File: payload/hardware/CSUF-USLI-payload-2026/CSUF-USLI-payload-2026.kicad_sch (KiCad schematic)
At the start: 1 part, among them U1 DEV-16771

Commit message: made some changes
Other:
- note added: "Leg Subsystem"
- note added: "Power Subsystem"
- note added: "Rover Subsystem"
- note added: "Sensor Subsystem"
- note added: "UTG Payload"
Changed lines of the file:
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@@
+		)
+	)
+	(polyline
+		(pts
+			(xy 284.48 59.69) (xy 284.48 59.69)
+		)
+		(stroke
+			(width 0.5)
+			(type default)
 		)
 	)
@@
 	(polyline
 		(pts
+			(xy 11.43 101.6) (xy 123.19 101.6)
+		)
+		(stroke
+			(width 0.5)
+			(type default)
+		)
+	)
+	(polyline
+		(pts
+			(xy 196.85 59.69) (xy 284.48 59.69)
+		)
+		(stroke
+			(width 0.5)
+			(type default)
+		)
+	)
+	(polyline
+		(pts
+			(xy 196.85 59.69) (xy 201.93 59.69)
+		)
+		(stroke
+			(width 0.5)
+			(type default)
+		)
+	)
+	(polyline
+		(pts
 			(xy 123.19 12.7) (xy 123.19 127)
 		)
@@
 		(effects
 			(font
+				(size 1.27 1.27)
+			)
+		)
+	)
+	(text "Rover Subsystem"
+		(exclude_from_sim no)
+		(at 37.084 177.292 0)
+		(effects
+			(font
+				(size 1.27 1.27)
+			)
+		)
+	)
+	(text "Power Subsystem"
+		(exclude_from_sim no)
+		(at 241.3 57.658 0)
+		(effects
+			(font
+				(size 1.27 1.27)
+			)
+		)
+	)
+	(text "Sensor Subsystem"
+		(exclude_from_sim no)
+		(at 69.85 97.79 0)
+		(effects
+			(font
+				(size 1.27 1.27)
+			)
+		)
+	)
+	(text "Leg Subsystem\n"
+		(exclude_from_sim no)
+		(at 37.338 182.372 0)
+		(effects
+			(font
+				(size 1.27 1.27)
+			)
+		)
+	)
+	(text "UTG Payload\n"
+		(exclude_from_sim no)
+		(at 193.548 189.992 0)
+		(effects
+			(font

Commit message: asdAdded changes n stuff
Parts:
- added BZ1: Buzzer, symbol Device:Buzzer
- added U2: GPS6MV2, symbol GPS6MV2:GPS6MV2
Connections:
- net +3V3: now also U2.1 (Vin)
- net GND: now also BZ1.2 (-), U2.4 (GND)
- net NEO6M_RX: now also U2.2 (RX)
- net NEO6M_TX: now also U2.3 (TX)
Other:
- note added: "I/O Subsystem"
- note removed: "Sensor Subsystem"

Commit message: Motor Diagram Concept
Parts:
- added D1: 12V Drill, symbol L298N Concept:12V_Drill
- added L1: L298N DualDC Motor Driver, symbol L298N Concept:L298N
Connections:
- net GND: now also L1. (Input1)
- new net: D1. (M2), L1. (Input1) (x2)
- new net 12V: L1. (Input1)
- new net Input1: L1. (Input1)
- new net Input2: L1. (Input1)
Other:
- note added: "Drill Controller Subsystem"

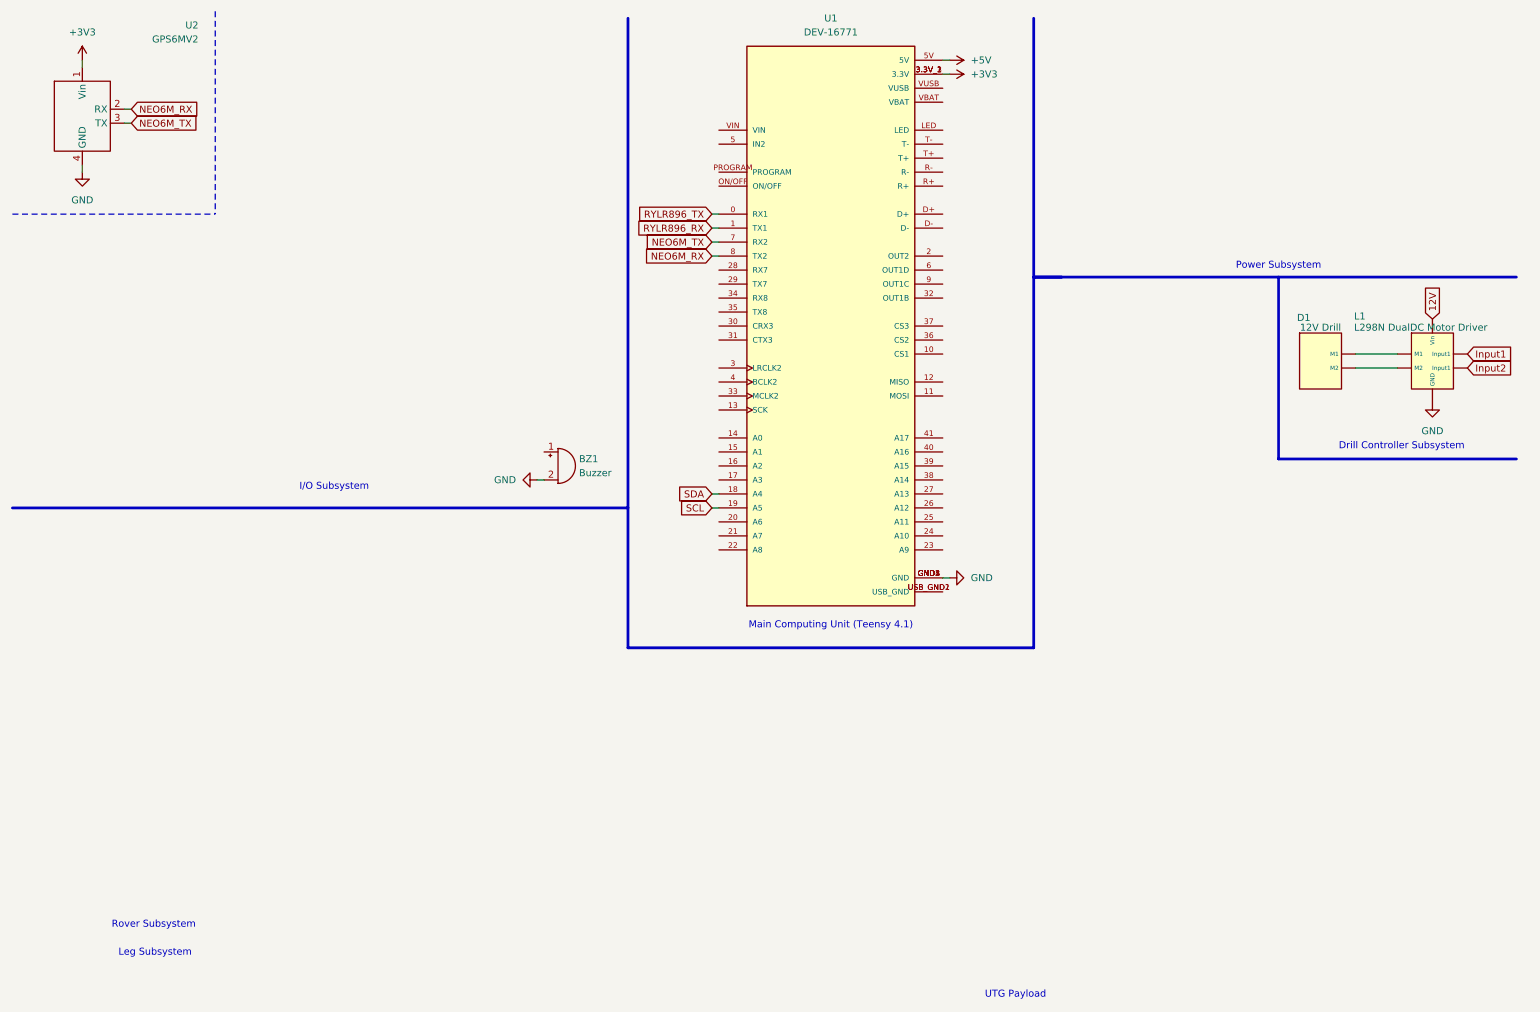
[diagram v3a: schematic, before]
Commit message: Added decoupling capacitors
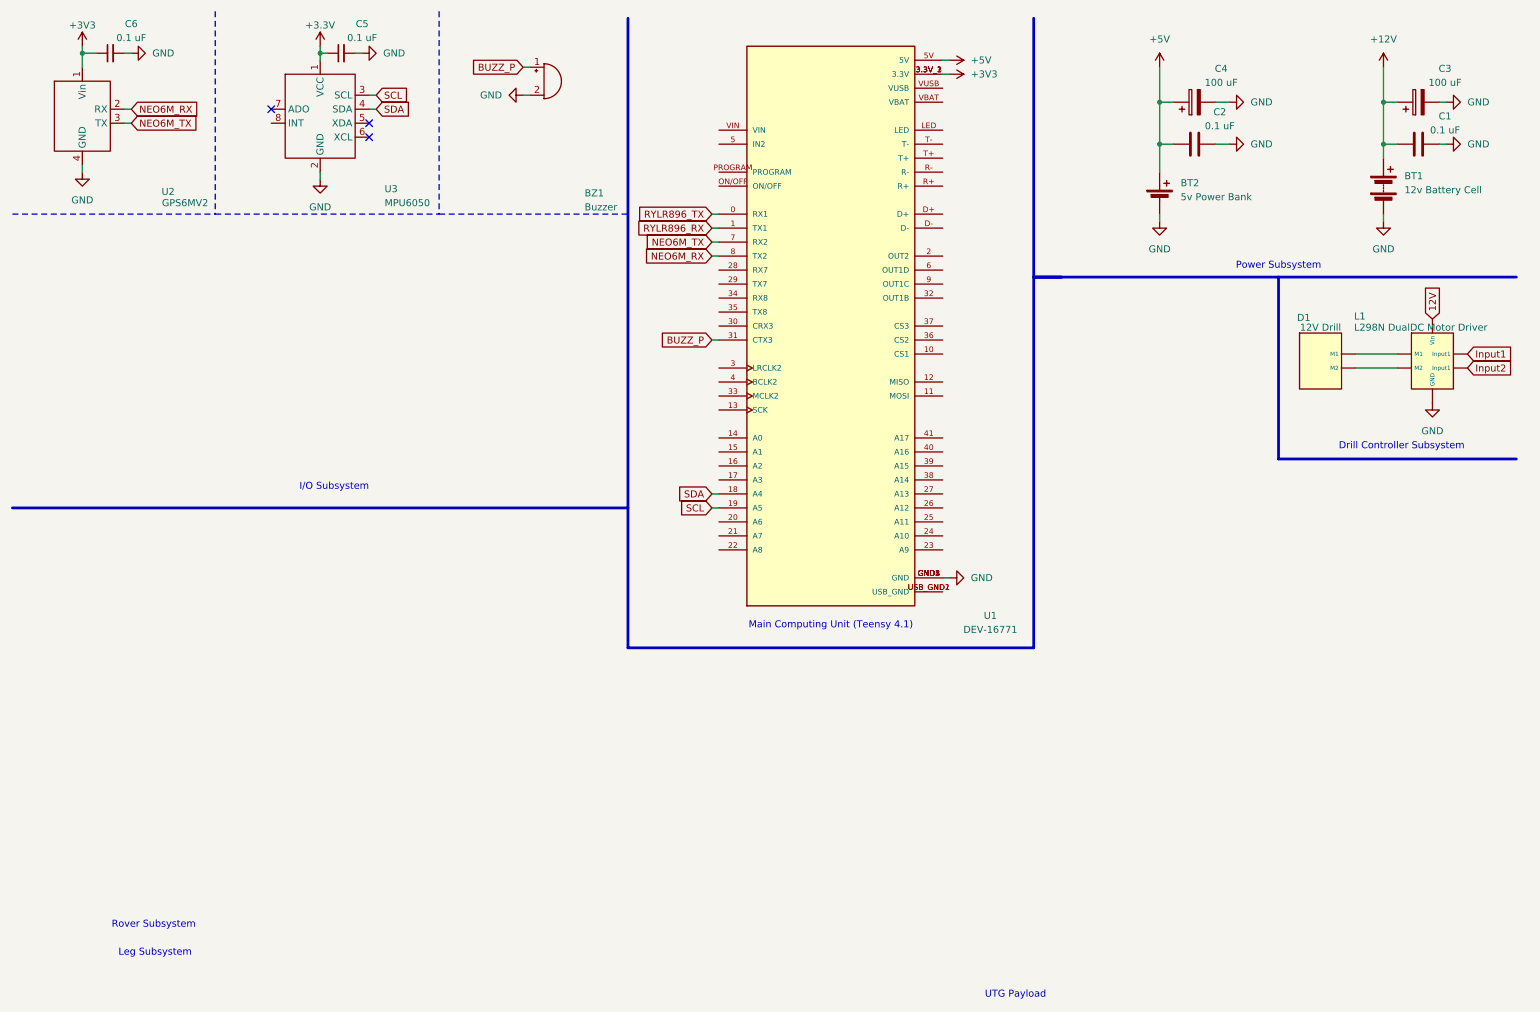
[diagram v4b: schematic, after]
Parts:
- added BT1: 12v Battery Cell, symbol Device:Battery
- added BT2: 5v Power Bank, symbol Device:Battery_Cell
- added C1, C2: 0.1 uF, symbol Device:C
- added C3, C4: 100 uF, symbol Device:C_Polarized
- added C5, C6: 0.1 uF, symbol Device:C_Small
- added U3: MPU6050, symbol MPU6050:MPU6050
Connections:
- net +3V3: now also C6.1
- net +5V: now also BT2.1 (+), C2.1, C4.1
- net GND: now also BT1.2 (-), BT2.2 (-), C1.2, C2.2, C3.2, C4.2, C5.2, C6.2, U3.2 (GND)
- net SCL: now also U3.3 (SCL)
- net SDA: now also U3.4 (SDA)
- net BUZZ_P: now reaches U1.31 (CTX3)
- net BUZZ_P: now also BZ1.1 (+)
- new net: D1. (M2), L1. (Input1)
- new net +12V: BT1.1 (+), C1.1, C3.1
- new net +3.3V: C5.1, U3.1 (VCC)
- no-connect marks 0 -> 3
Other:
- moved on the sheet: BZ1

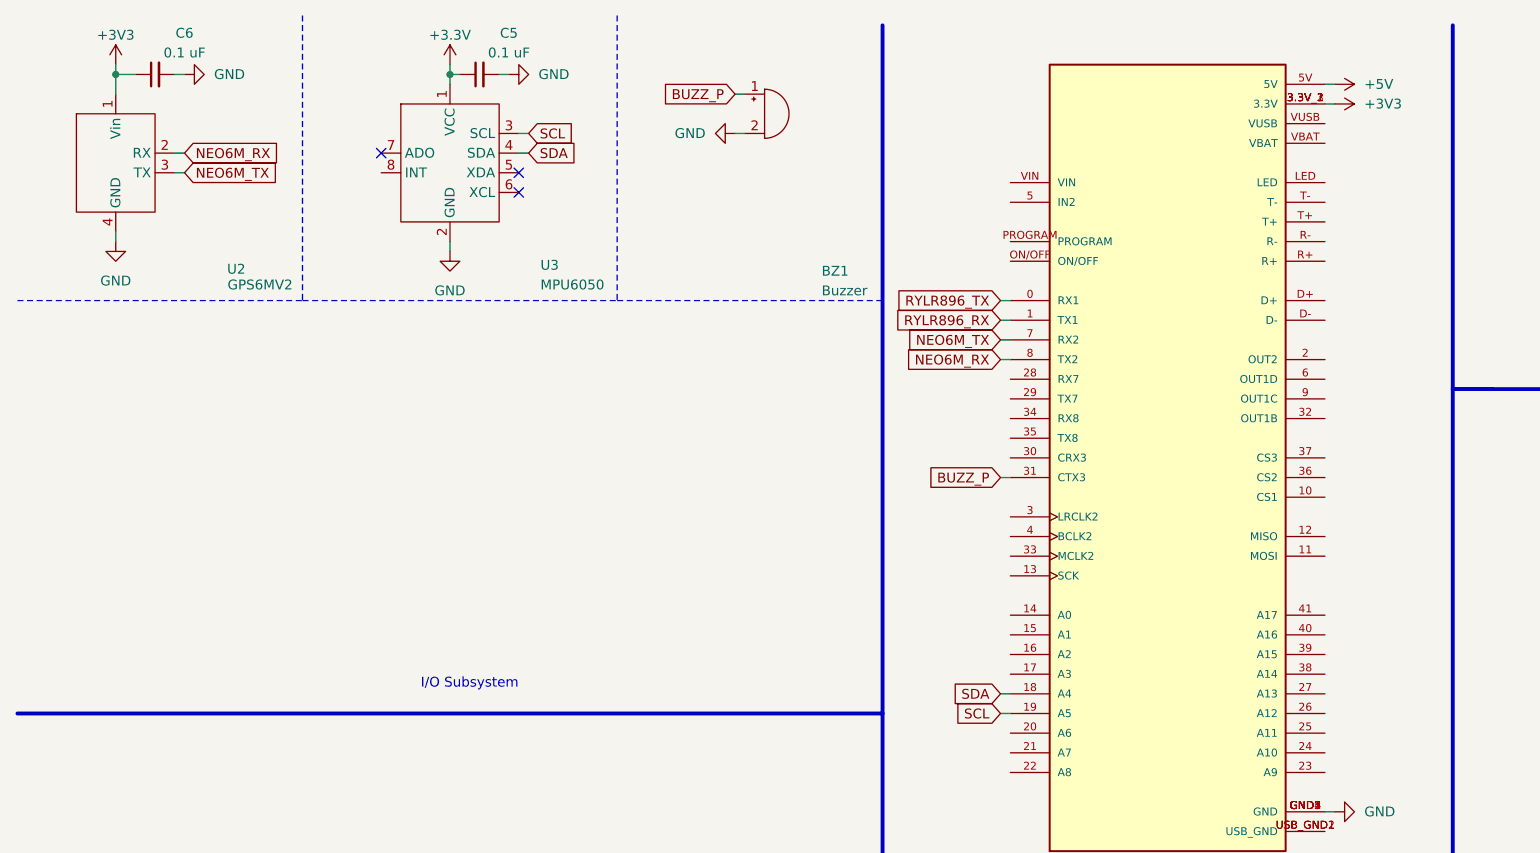
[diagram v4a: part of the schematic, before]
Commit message: added BMP280
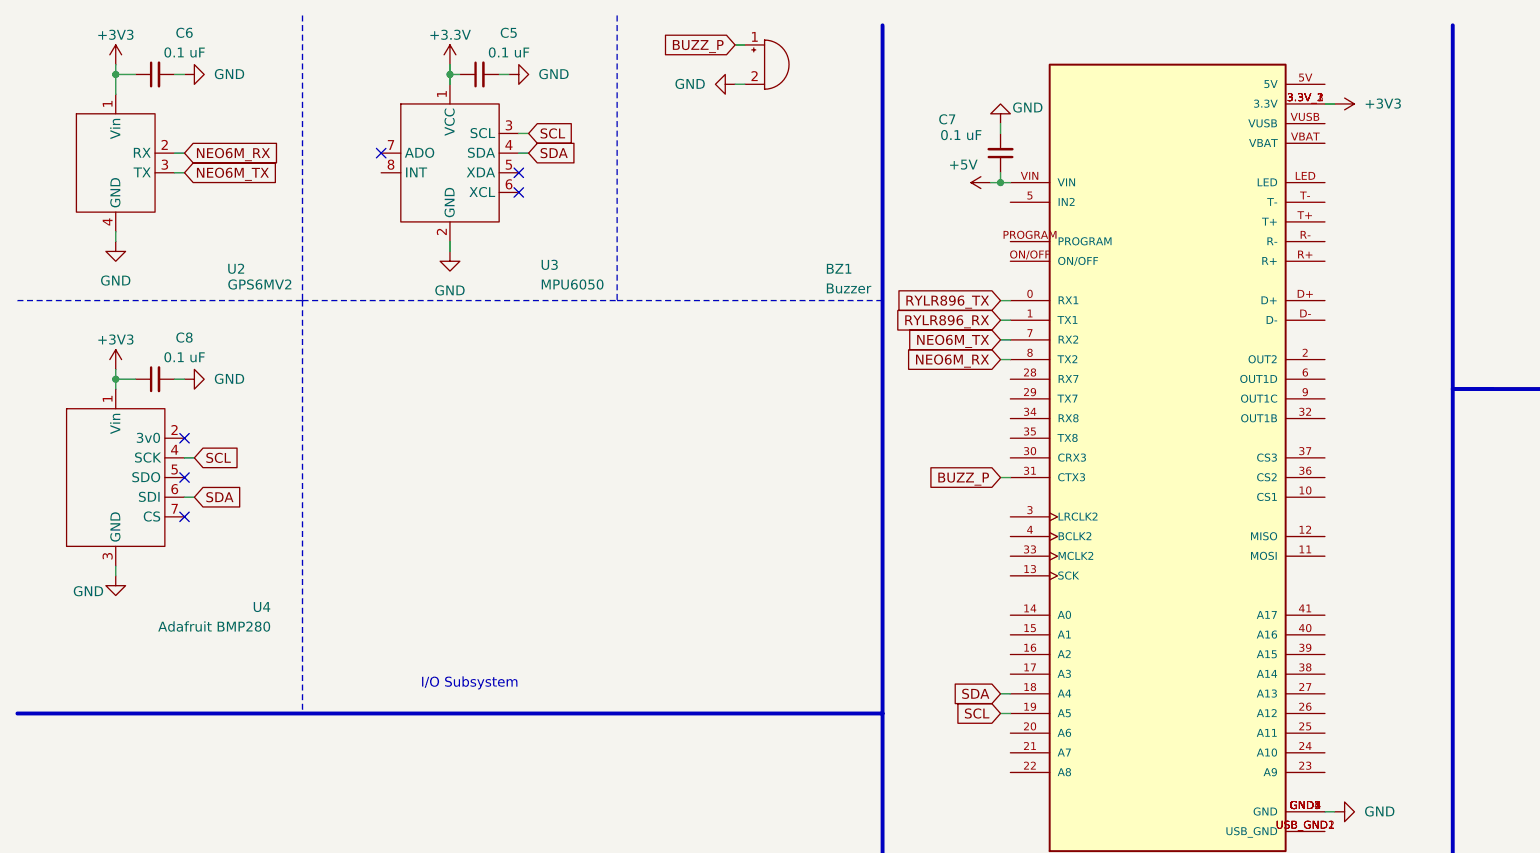
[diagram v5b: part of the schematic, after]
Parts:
- added C7, C8: 0.1 uF, symbol Device:C_Small
- added U4: Adafruit BMP280, symbol BMP280:Adafruit_BMP280
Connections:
- net +3V3: now also C8.1, U4.1 (Vin)
- net +5V: now also U1.VIN, C7.1; no longer U1.5V
- net GND: now also C7.2, C8.2, U4.3 (GND)
- net SCL: now also U4.4 (SCK)
- net SDA: now also U4.6 (SDI)
- new net: D1. (M2), L1. (Input1)
- no-connect marks 3 -> 6
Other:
- moved on the sheet: BZ1

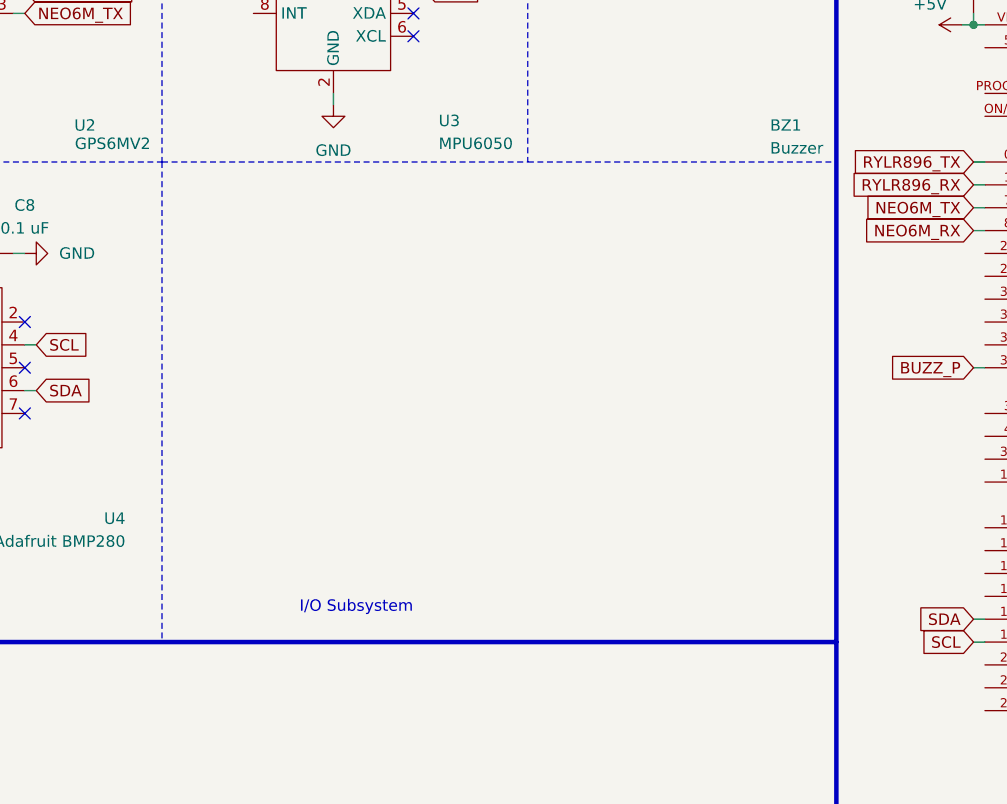
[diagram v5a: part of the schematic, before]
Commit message: Added the final soil sensors
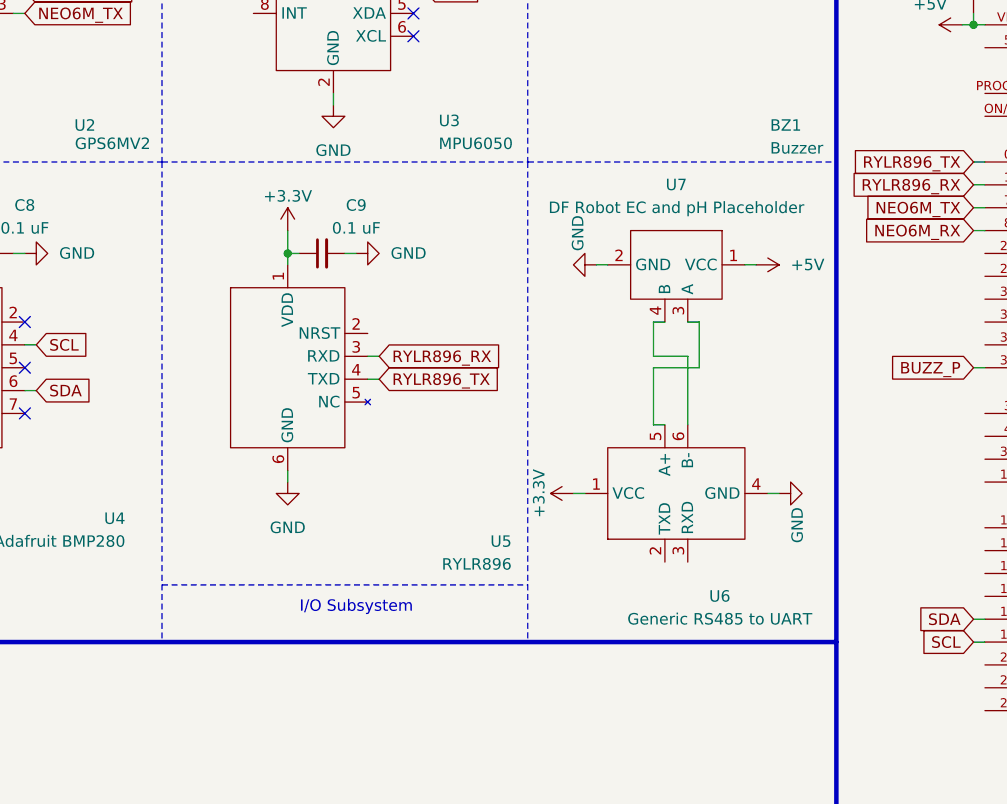
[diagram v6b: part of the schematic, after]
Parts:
- added C9: 0.1 uF, symbol Device:C_Small
- added U5: RYLR896, symbol RYLR896:RYLR896
- added U6: Generic RS485 to UART, symbol RS485_to_UART:Generic_RS485_to_UART
- added U7: DF Robot EC and pH Placeholder, symbol Soil_Sensors:DFRobot_EC_and_pH
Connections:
- net +3.3V: now also C9.1, U5.1 (VDD), U6.1 (VCC)
- net +5V: now also U7.1 (VCC)
- net GND: now also C9.2, U5.6 (GND), U6.4 (GND), U7.2 (GND)
- net RYLR896_RX: now also U5.3 (RXD)
- net RYLR896_TX: now also U5.4 (TXD)
- new net: D1. (M2), L1. (Input1)
- new net: U6.5 (A+), U7.3 (A)
- new net: U6.6 (B-), U7.4 (B)

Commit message: idk what change i did
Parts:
- BT1: value 12v Battery Cell -> 13.3v Battery Cell
- D1: value 12V Drill -> Drill
- L1: value L298N DualDC Motor Driver -> Generic Motor Driver
- U4: value Adafruit BMP280 -> Adafruit BMP390
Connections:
- net 12V is gone; now on net Input2: L1. (Input1)
- net +12V renamed +13.3V
- net +13.3V: now also L1. (Input1)
- new net: D1. (M2), L1. (Input1)
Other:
- note added: "Drill Subsystem"
- note removed: "Drill Controller Subsystem"
- moved on the sheet: BT1, BT2, BZ1, C1, C2, C3, C4, C5, C6, C8, C9, D1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
